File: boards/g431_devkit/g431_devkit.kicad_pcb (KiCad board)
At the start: 2 copper layers, 95.6 x 92.6 mm, 18 parts, among them J1 samtec_ftsh_107_01_l_dv_k, J1 usb_c_16p, U1 VAL**, U1 ht7333

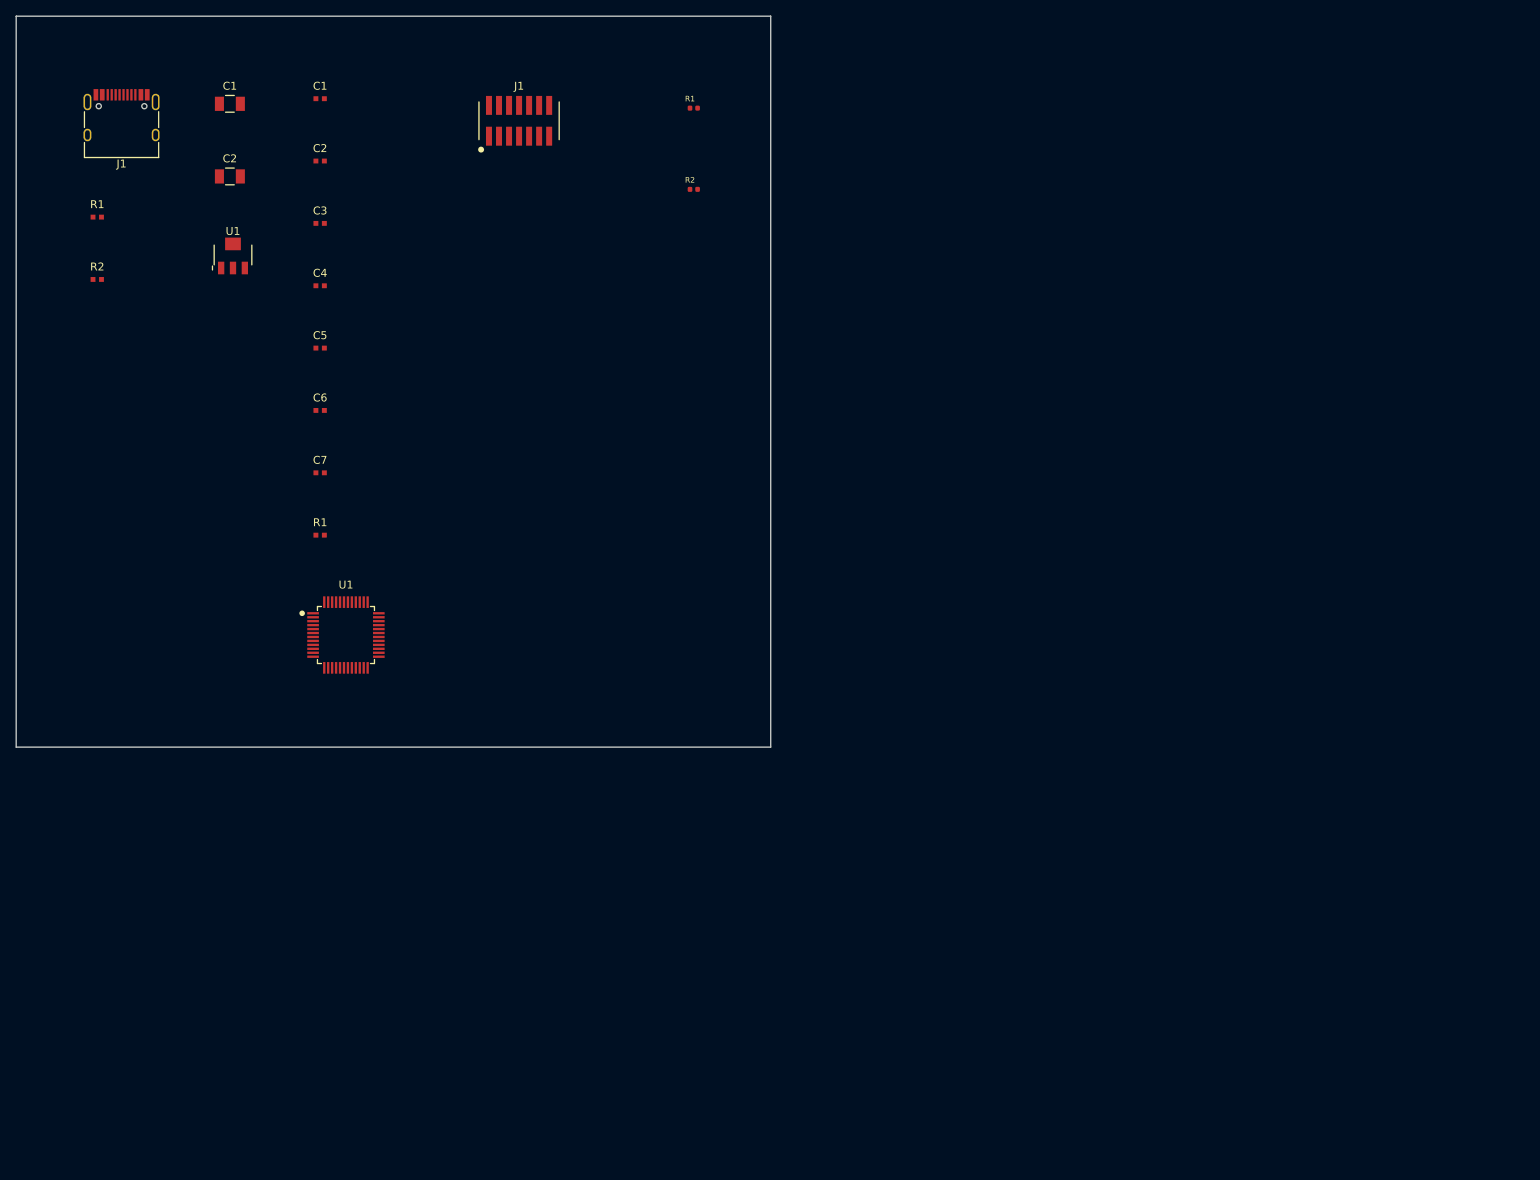
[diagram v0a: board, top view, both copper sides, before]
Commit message: PCB 배치 규칙집 P1~P4 + build_pcb 반영 (g431_devkit rev 0.2)
- rules/pcb-layout.md 신설 (사용자 확정 원문 인용): P1 외곽 선언 우선,
  잠정 산정 시 용지 중앙 / P2 커넥터 가장자리, 삽입구는 보드 밖 /
  P3 디버그 커넥터 MCU 근처 / P4 층수 사전 확인.
- build_pcb: 용지(A4) 중앙 평행이동, USB 리셉터클 90도 회전+왼변 스냅,
  블록 열 순서로 P3 충족, board.json layers(=2) 반영.
- 게이트 재통과 (ERC 0 / 넷 10 / DRC 0).

Co-Authored-By: Claude Fable 5 <noreply@anthropic.com>
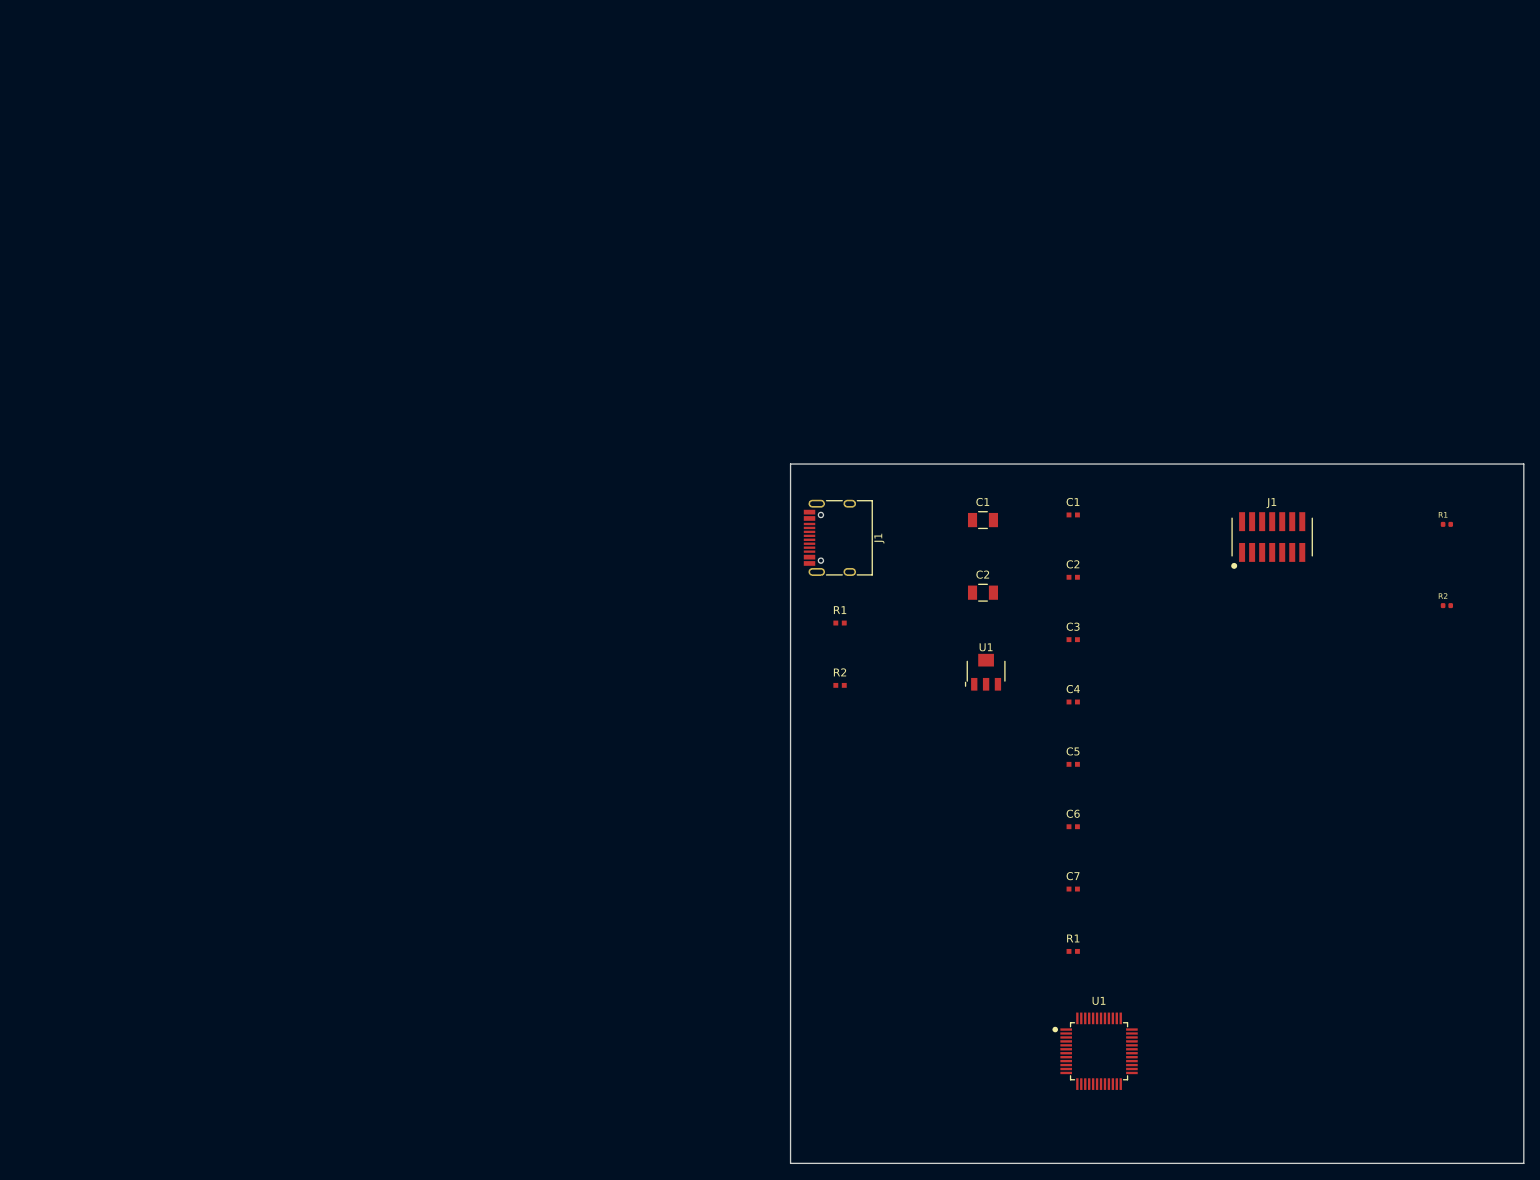
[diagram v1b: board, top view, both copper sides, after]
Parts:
- removed the C1 at (42.5, 14.4)
- removed the C1 at (31.1, 15.1)
- removed the C2 at (31.1, 24.3)
- removed the C2 at (42.5, 22.3)
- removed the J1 at (17.3, 18.0)
- removed the J1 at (67.7, 17.2)
- removed the R1 at (89.8, 15.6)
- removed the R1 at (42.5, 69.7)
- removed the R1 at (14.3, 29.4)
- removed the R2 at (89.8, 25.9)
- removed the R2 at (14.3, 37.3)
- removed the U1 at (31.5, 34.2)
- removed the U1 at (45.8, 82.4)
- added C1: VAL**, antmicro_cl05a104ka5nnnc, F.Cu at (137.9, 67.2)
- added C1: VAL**, antmicro_c3216x7r1h106k160ae, F.Cu at (126.4, 67.8)
- added C2: VAL**, antmicro_cl05a104ka5nnnc, F.Cu at (137.9, 75.1)
- added C2: VAL**, antmicro_c3216x7r1h106k160ae, F.Cu at (126.4, 77.0)
- added J1: usb_c_16p, usb_c_16p, F.Cu at (108.5, 70.1)
- added J1: samtec_ftsh_107_01_l_dv_k, samtec_ftsh_107_01_l_dv_k, F.Cu at (163.1, 70.0)
- added R1: R_0402_1005Metric, antmicro_crcw04021k80fkedc, F.Cu at (185.2, 68.4)
- added R1: VAL**, vishay_crcw040210k0fked, F.Cu at (137.9, 122.4)
- added R1: VAL**, vishay_crcw04025k10fked, F.Cu at (108.3, 80.9)
- added R2: R_0402_1005Metric, antmicro_crcw04021k80fkedc, F.Cu at (185.2, 78.6)
- added R2: VAL**, vishay_crcw04025k10fked, F.Cu at (108.3, 88.8)
- added U1: ht7333, ht7333, F.Cu at (126.8, 87.0)
- added U1: VAL**, stm32g431cbtx, F.Cu at (141.1, 135.1)
- moved C3 109.0 mm to (137.9, 83.0)
- moved C5 109.0 mm to (137.9, 98.7)
- moved C6 109.0 mm to (137.9, 106.6)
- moved C7 109.0 mm to (137.9, 114.5)
- moved C4 109.0 mm to (137.9, 90.9)
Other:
- board size 95.6 x 92.6 mm -> 92.9 x 88.6 mm

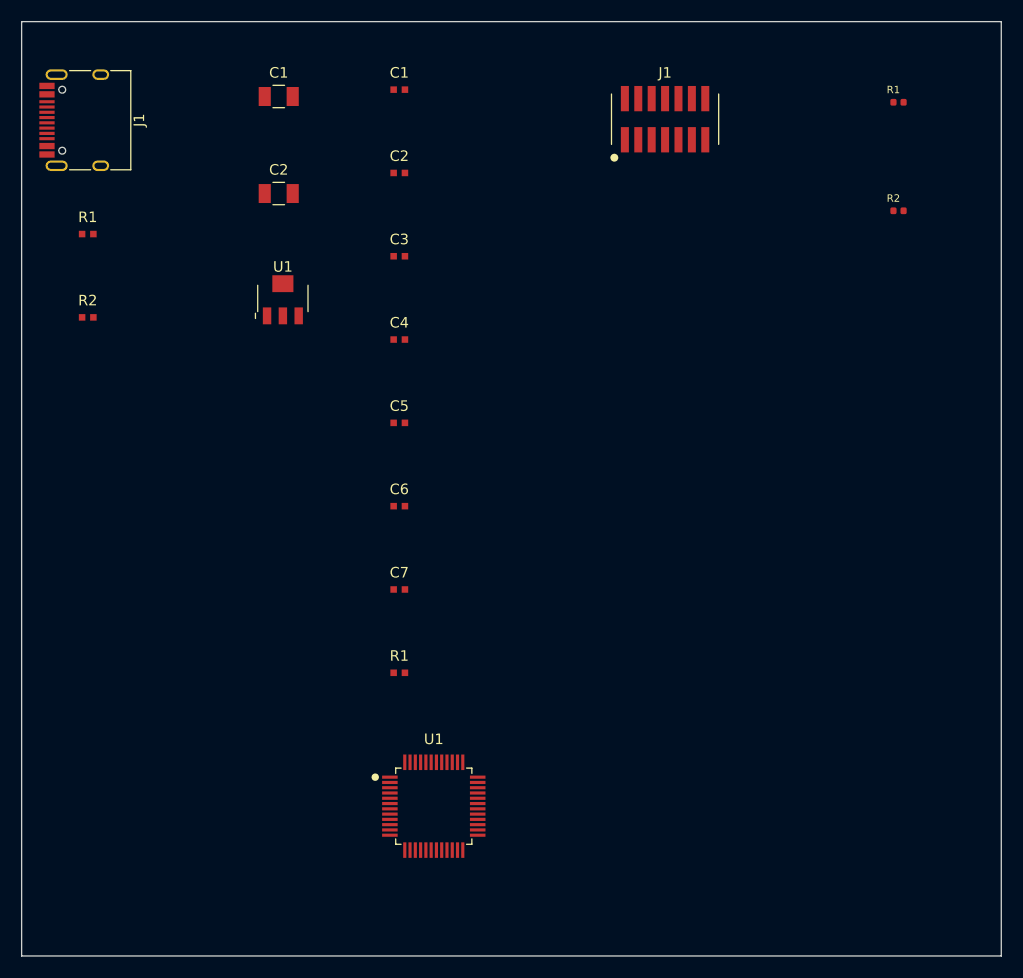
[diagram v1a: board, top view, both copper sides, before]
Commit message: P1/P2 교정: USB 방향 실측 수정(회전 270) + 외곽 최소화 53x33
- USB 리셉터클: KiCad 양수 회전=화면 반시계 — 90도가 패드를 가장자리로
  보내던 것을 실측으로 확인, 270으로 교정 (패드 안쪽/입 바깥).
- P1 교정 반영: 외곽 = 부품+배선 여유 최소 (여백 1.0/블록 2.5/외곽 2.5,
  세로 32mm 감기, 글자 제외 실몸체 기준) — 93x89 -> 53x33mm.
- 초기화 REF 글자는 F.Fab (실크 REF가 이웃 패드 무는 DRC 19건 —
  P5 후보로 기록, 사용자 확인 대기). DRC 위반 0 재통과.

Co-Authored-By: Claude Fable 5 <noreply@anthropic.com>
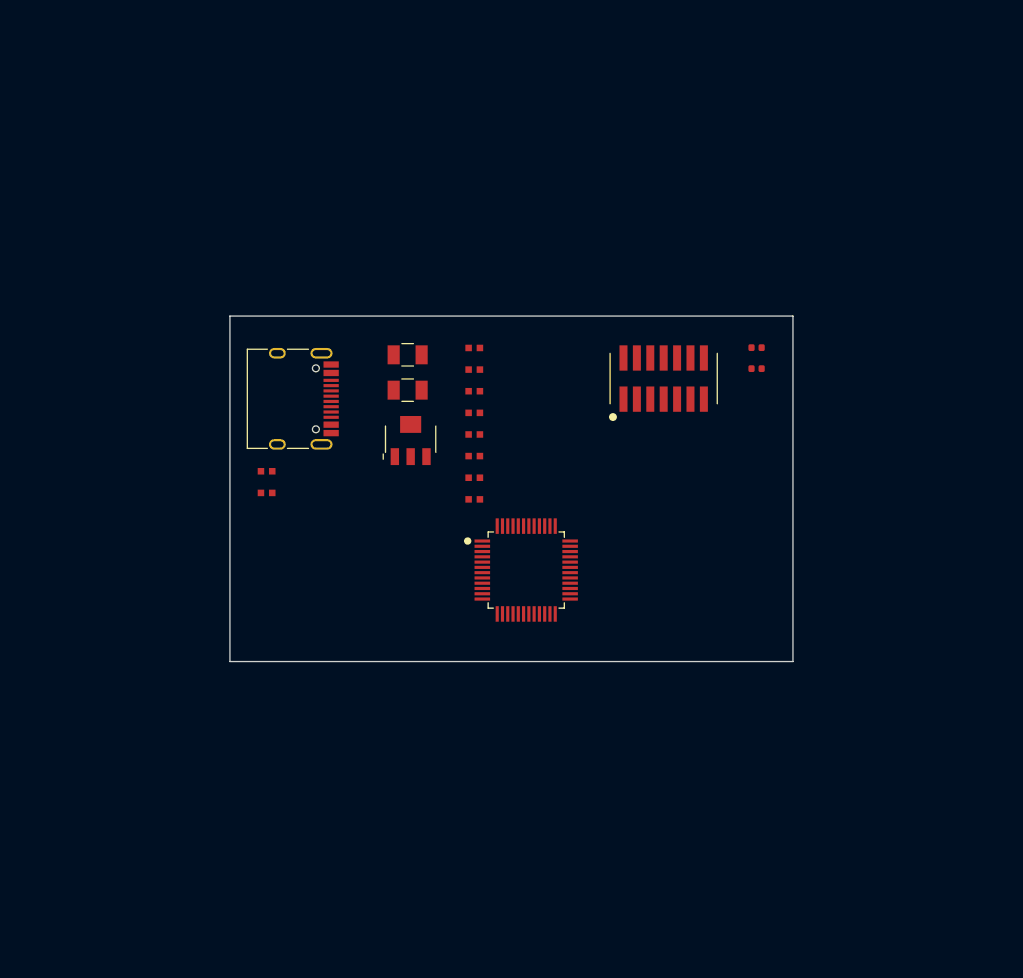
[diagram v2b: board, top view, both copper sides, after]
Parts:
- removed the C1 at (137.9, 67.2)
- removed the C1 at (126.4, 67.8)
- removed the C2 at (137.9, 75.1)
- removed the C2 at (126.4, 77.0)
- removed the J1 at (108.5, 70.1)
- removed the J1 at (163.1, 70.0)
- removed the R1 at (185.2, 68.4)
- removed the R1 at (137.9, 122.4)
- removed the R1 at (108.3, 80.9)
- removed the R2 at (185.2, 78.6)
- removed the R2 at (108.3, 88.8)
- removed the U1 at (126.8, 87.0)
- removed the U1 at (141.1, 135.1)
- added C1: VAL**, antmicro_c3216x7r1h106k160ae, F.Cu at (138.7, 92.3)
- added C1: VAL**, antmicro_cl05a104ka5nnnc, F.Cu at (145.0, 91.7)
- added C2: VAL**, antmicro_c3216x7r1h106k160ae, F.Cu at (138.7, 95.7)
- added C2: VAL**, antmicro_cl05a104ka5nnnc, F.Cu at (145.0, 93.7)
- added J1: samtec_ftsh_107_01_l_dv_k, samtec_ftsh_107_01_l_dv_k, F.Cu at (162.9, 94.5)
- added J1: usb_c_16p, usb_c_16p, F.Cu at (127.4, 96.5)
- added R1: VAL**, vishay_crcw04025k10fked, F.Cu at (125.3, 103.3)
- added R1: VAL**, vishay_crcw040210k0fked, F.Cu at (145.0, 106.0)
- added R1: R_0402_1005Metric, antmicro_crcw04021k80fkedc, F.Cu at (171.7, 91.6)
- added R2: VAL**, vishay_crcw04025k10fked, F.Cu at (125.3, 105.4)
- added R2: R_0402_1005Metric, antmicro_crcw04021k80fkedc, F.Cu at (171.7, 93.6)
- added U1: VAL**, stm32g431cbtx, F.Cu at (149.9, 112.7)
- added U1: ht7333, ht7333, F.Cu at (138.9, 100.3)
- moved C3 14.6 mm to (145.0, 95.8)
- moved C7 12.8 mm to (145.0, 104.0)
- moved C4 9.94 mm to (145.0, 97.8)
- moved C6 8.55 mm to (145.0, 101.9)
- moved C5 7.19 mm to (145.0, 99.8)
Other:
- board size 92.9 x 88.6 mm -> 53.4 x 32.8 mm

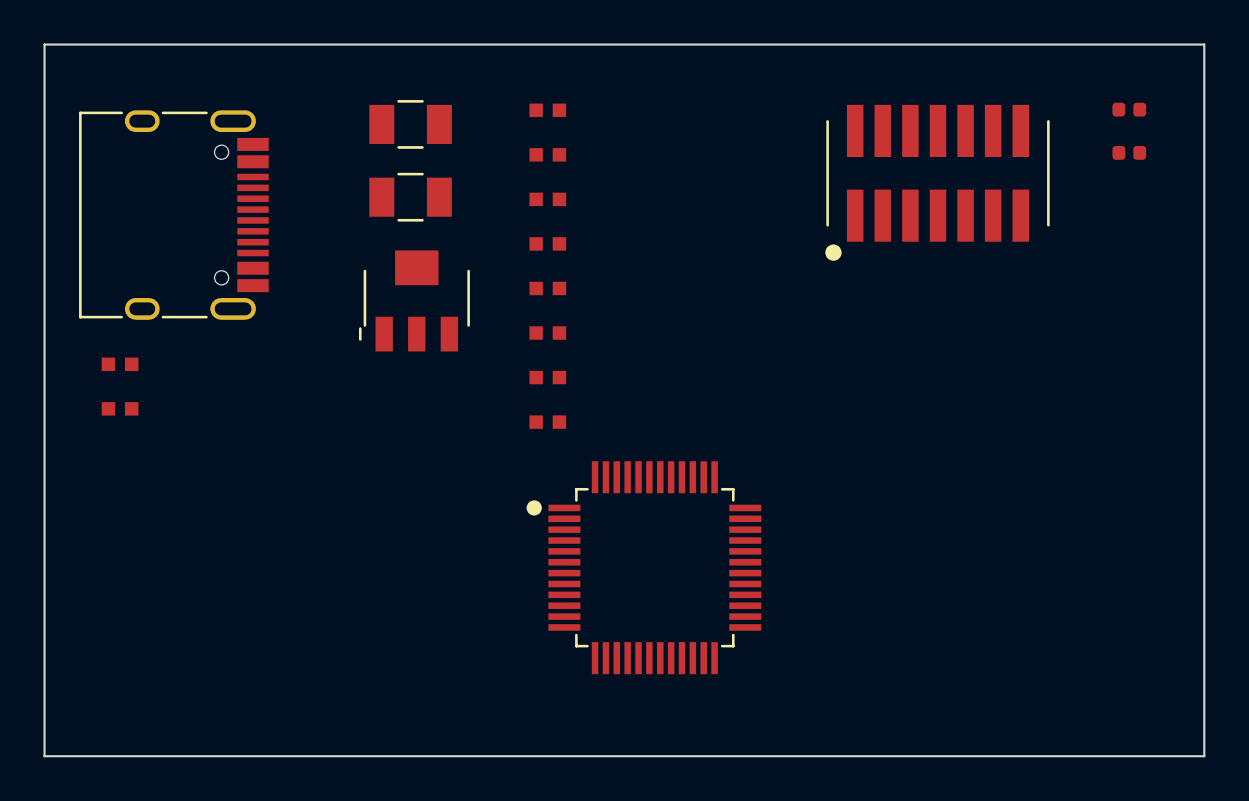
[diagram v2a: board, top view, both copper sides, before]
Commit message: P6/P7: edge_face 메타 + 기능 군집 배치 (외곽 40x29)
- P6: 가장자리 접면을 부품 데이터(meta.parameters.edge_face)에 표기 —
  usb_c_16p '+y'. 배치기는 id 추측 대신 메타를 읽어 회전하고 실크를
  외곽선에 일치 스냅.
- P7: 메인 IC(최다핀) 군집 중앙 — IC 가운데 + 수동소자 좌우 열,
  나머지 블록 군집을 사방 밀착 (가장자리 군집은 해당 변).
  외곽 53x33 -> 40x29mm, 빈공간 최소화. DRC 0 유지.

Co-Authored-By: Claude Fable 5 <noreply@anthropic.com>
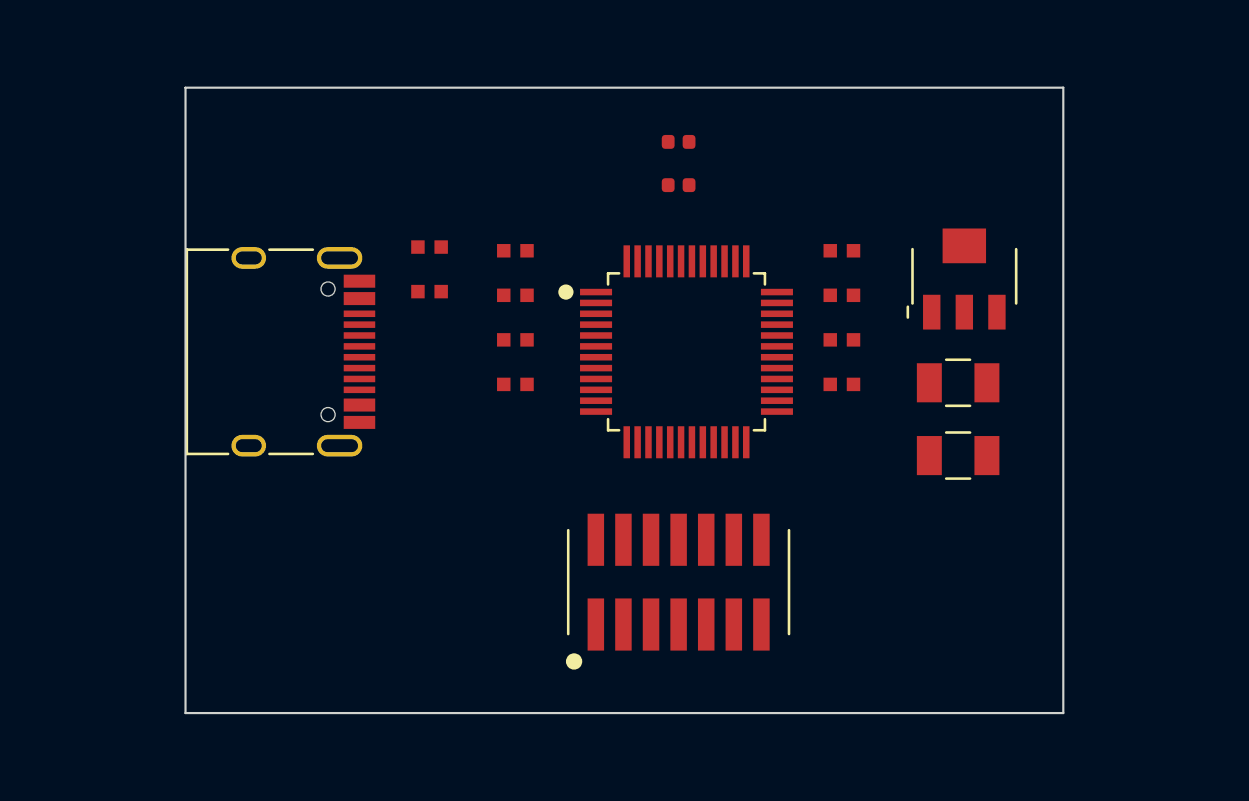
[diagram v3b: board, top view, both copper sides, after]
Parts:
- removed the C1 at (138.7, 92.3)
- removed the C1 at (145.0, 91.7)
- removed the C2 at (138.7, 95.7)
- removed the C2 at (145.0, 93.7)
- removed the J1 at (162.9, 94.5)
- removed the J1 at (127.4, 96.5)
- removed the R1 at (125.3, 103.3)
- removed the R1 at (145.0, 106.0)
- removed the R1 at (171.7, 91.6)
- removed the R2 at (125.3, 105.4)
- removed the R2 at (171.7, 93.6)
- removed the U1 at (149.9, 112.7)
- removed the U1 at (138.9, 100.3)
- added C1: VAL**, antmicro_c3216x7r1h106k160ae, F.Cu at (163.9, 104.2)
- added C1: VAL**, antmicro_cl05a104ka5nnnc, F.Cu at (158.5, 98.1)
- added C2: VAL**, antmicro_cl05a104ka5nnnc, F.Cu at (143.5, 98.1)
- added C2: VAL**, antmicro_c3216x7r1h106k160ae, F.Cu at (163.9, 107.5)
- added J1: usb_c_16p, usb_c_16p, F.Cu at (132.3, 102.8)
- added J1: samtec_ftsh_107_01_l_dv_k, samtec_ftsh_107_01_l_dv_k, F.Cu at (151.0, 113.4)
- added R1: R_0402_1005Metric, antmicro_crcw04021k80fkedc, F.Cu at (151.0, 93.1)
- added R1: VAL**, vishay_crcw040210k0fked, F.Cu at (143.5, 104.3)
- added R1: VAL**, vishay_crcw04025k10fked, F.Cu at (139.5, 97.9)
- added R2: R_0402_1005Metric, antmicro_crcw04021k80fkedc, F.Cu at (151.0, 95.1)
- added R2: VAL**, vishay_crcw04025k10fked, F.Cu at (139.5, 100.0)
- added U1: ht7333, ht7333, F.Cu at (164.1, 99.3)
- added U1: VAL**, stm32g431cbtx, F.Cu at (151.4, 102.8)
- moved C3 14.2 mm to (158.5, 100.2)
- moved C5 13.7 mm to (158.5, 102.2)
- moved C7 13.5 mm to (158.5, 104.3)
- moved C4 2.80 mm to (143.5, 100.2)
- moved C6 1.53 mm to (143.5, 102.2)
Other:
- board size 53.4 x 32.8 mm -> 40.4 x 28.8 mm
